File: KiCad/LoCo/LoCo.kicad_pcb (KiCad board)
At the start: 2 copper layers, 72 x 121.9 mm, 97 parts, among them J1 Conn_01x04, P1 Cart Connector, P3 Conn_01x06, P5 Conn_01x05, Q2 2SC4081, SW2 Right, SW3 Down, SW4 Up, SW5 Left, SW6 A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

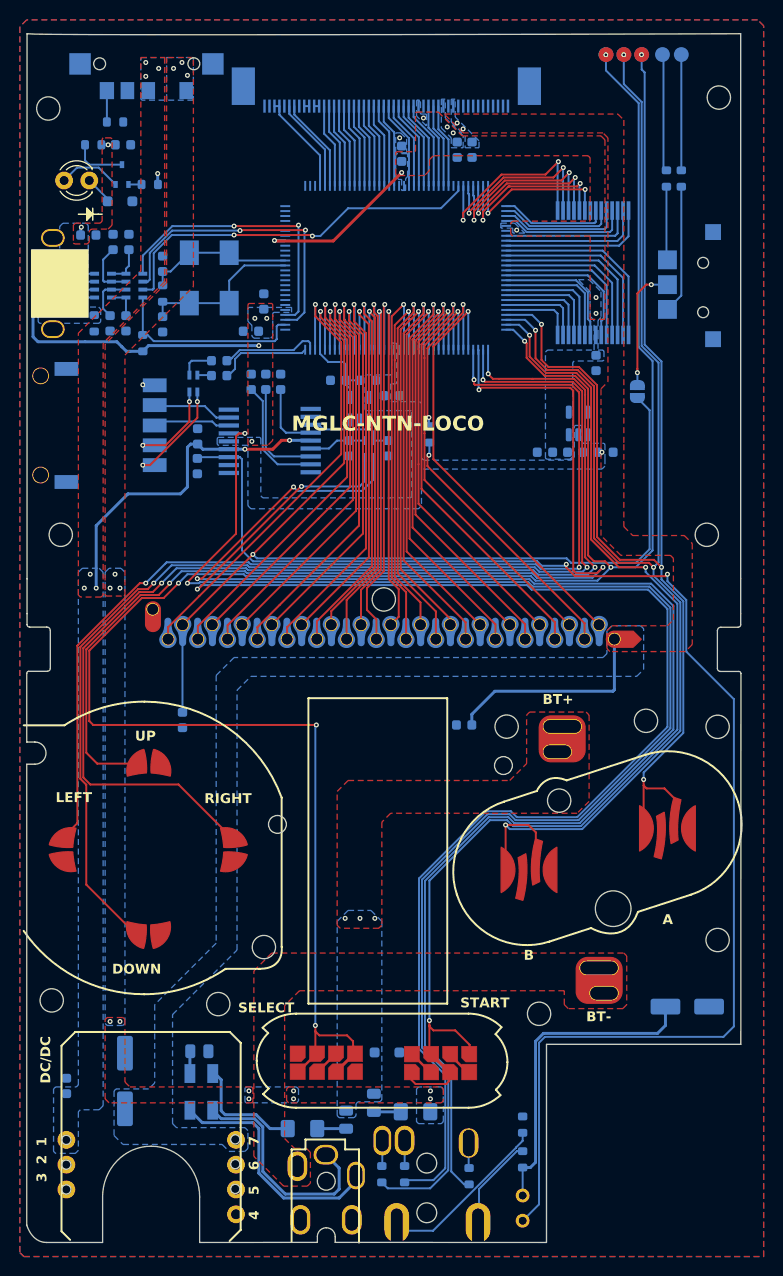
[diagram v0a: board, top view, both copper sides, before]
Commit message: changed cpu footprint
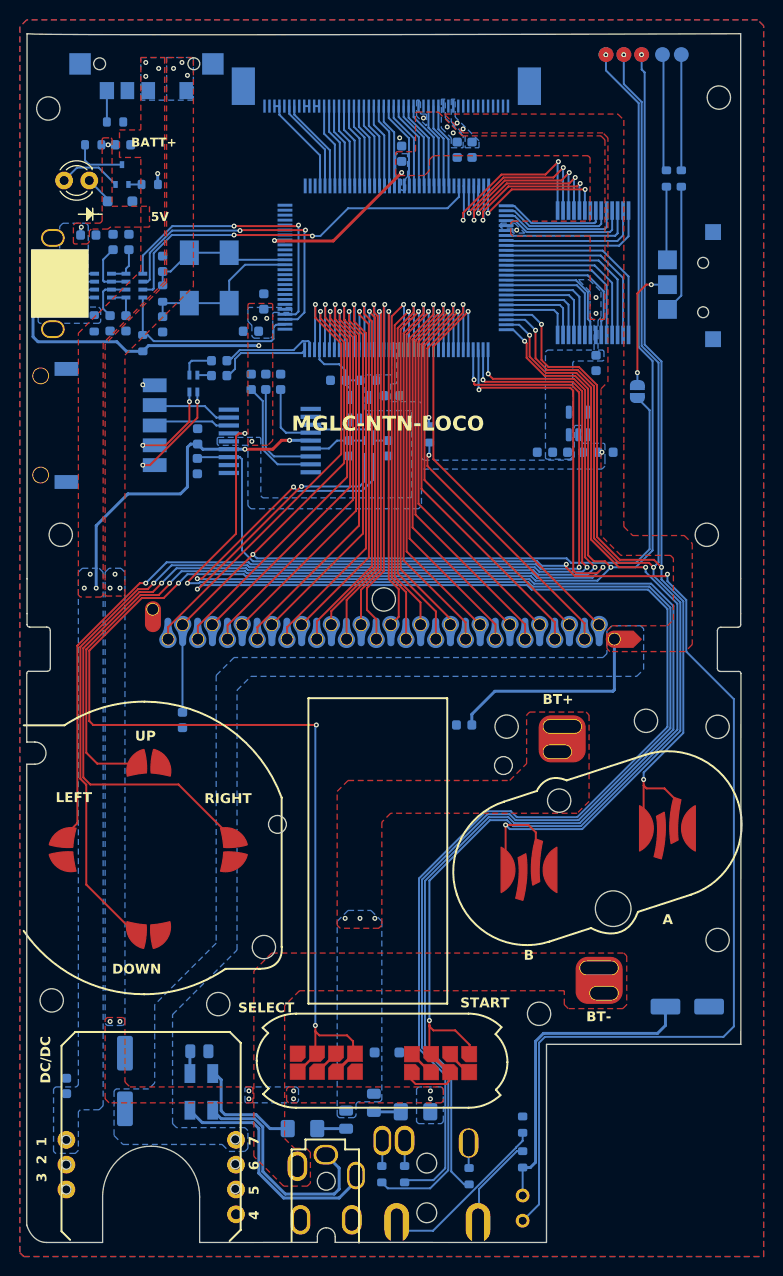
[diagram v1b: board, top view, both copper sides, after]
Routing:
- net /CGB_Controls/P10: track 125.4 -> 122.5 mm
- net Net-(U1A-XTAL2): track 14.9 -> 13.8 mm
- net Net-(RA2A-R1.1): track 8.97 -> 8.16 mm
- net Net-(D4-K): track 3.36 -> 2.62 mm
- net Net-(EM10-Pad1): track 24.3 -> 23.7 mm
- net Net-(U3-RIN): track 7.80 -> 7.24 mm
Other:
- board text added: "5V"
- board text added: "BATT+"
- board text added: "V1.2"
- board text removed: "V1.1"
